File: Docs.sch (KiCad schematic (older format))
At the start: 0 parts

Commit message: Merge branch 'dev-GW4203B-1.2' of https://github.com/garrettsworkshop/RAM2E into dev-GW4203B-1.2
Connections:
- wire segments 411 -> 536
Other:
- note added: "CKE (idle)"
- note added: "CKE (read/write)"
- note added: "CMD (idle)"
- note added: "DQMH"
- note added: "DQML"
- note removed: "CKE"
- note removed: "DQMH/L"
- note removed: "old read data"

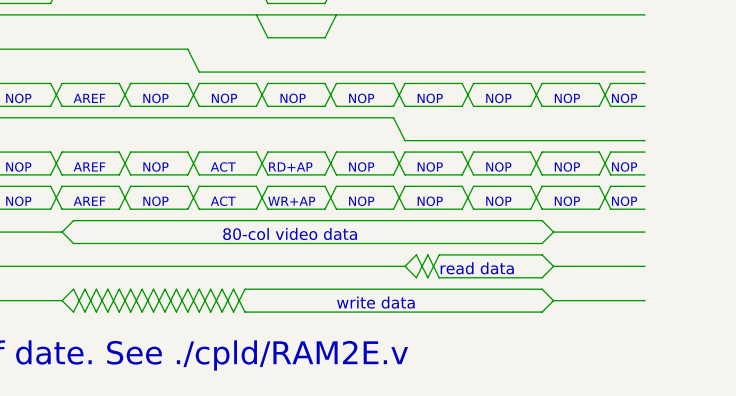
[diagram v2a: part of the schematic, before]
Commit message: Update timing diagram in schematic
Now reflects longer MAX V propagation delays
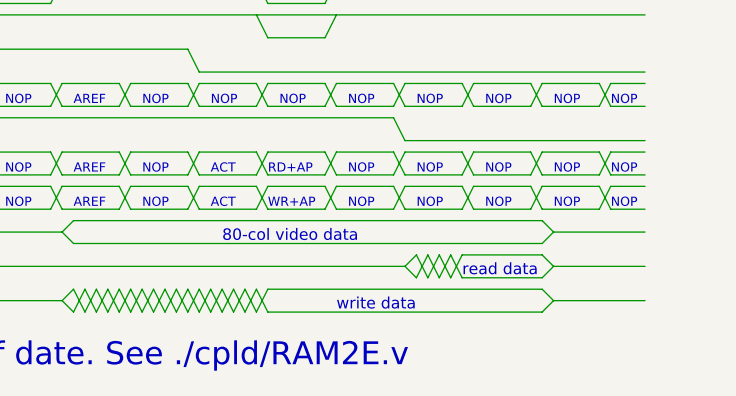
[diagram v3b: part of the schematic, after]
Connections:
- wire segments 536 -> 544
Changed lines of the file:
@@
 	3650 3450 4100 3450
 Wire Wire Line
-	7000 3350 8300 3350
-Wire Wire Line
-	7000 3450 8300 3450
+	7100 3350 8300 3350
+Wire Wire Line
+	7100 3450 8300 3450
 Text Notes 4150 3700 0    100  ~ 0
 Information may be out of date. See ./cpld/RAM2E.v
-Text Notes 7850 3300 0    50   ~ 0
+Text Notes 7950 3300 0    50   ~ 0
 read data
 Wire Wire Line
-	7850 3300 8300 3300
-Wire Wire Line
-	7850 3200 8300 3200
+	7950 3300 8300 3300
 Text Notes 7400 3450 0    50   ~ 0
 write data
@@
 	7750 3300 7800 3200
 Wire Wire Line
-	7800 3200 7850 3300
-Wire Wire Line
-	7800 3300 7850 3200
-Wire Wire Line
 	8050 1850 8100 1950
 Wire Wire Line
@@
 	6900 3450 6950 3350
 Wire Wire Line
+	6200 3400 4150 3400
+Wire Wire Line
+	6200 3400 6250 3350
+Wire Wire Line
+	7800 3200 7850 3300
+Wire Wire Line
+	7800 3300 7850 3200
+Wire Wire Line
+	7850 3200 7900 3300
+Wire Wire Line
+	7850 3300 7900 3200
+Wire Wire Line
+	7950 3200 8300 3200
+Wire Wire Line
+	7900 3200 7950 3300
+Wire Wire Line
+	7900 3300 7950 3200
+Wire Wire Line
 	6950 3350 7000 3450
 Wire Wire Line
 	6950 3450 7000 3350
 Wire Wire Line
-	6200 3400 4150 3400
-Wire Wire Line
-	6200 3400 6250 3350
+	7000 3350 7050 3450
+Wire Wire Line
+	7000 3450 7050 3350
+Wire Wire Line
+	7050 3350 7100 3450
+Wire Wire Line
+	7050 3450 7100 3350
 $EndSCHEMATC
